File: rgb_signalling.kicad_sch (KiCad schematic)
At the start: 7 parts, among them IC1 TXB0108PWR

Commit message: working on board
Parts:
- C2, C3, C4: footprint (none) -> Capacitor_SMD:C_0504_1310Metric_Pad0.83x1.28mm_HandSolder
- renumbered D1 to D2, D2 to D3, D3 to D4
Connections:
- no-connect marks 9 -> 15
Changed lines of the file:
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@@
+	)
+	(no_connect
+		(at 154.94 55.88)
 	)
 	(no_connect
@@
 	)
 	(no_connect
+		(at 154.94 53.34)
+	)
+	(no_connect
+		(at 154.94 45.72)
+	)
+	(no_connect
+		(at 154.94 48.26)
+	)
+	(no_connect
 		(at 127 40.64)
+	)
+	(no_connect
+		(at 154.94 43.18)
 	)
 	(no_connect
 		(at 154.94 40.64)
+	)
+	(no_connect
+		(at 154.94 50.8)
 	)
 	(no_connect
@@
 		(dnp no)
 		(fields_autoplaced yes)
-		(property "Reference" "#PWR07"
+		(property "Reference" "#PWR09"
 			(at 156.21 120.65 0)
 			(effects
@@
 			(project "edge_human_detection_board"
 				(path "/f7edb1cc-a42a-4cc0-9a6f-d9bd2b944353/381303fc-36c2-4b05-8887-9e7cf2e23d0c"
-					(reference "#PWR07")
+					(reference "#PWR09")
 					(unit 1)
 				)
@@
 	(symbol
 		(lib_id "Device:C")
-		(at 198.12 111.76 180)
+		(at 175.26 92.71 180)
 		(unit 1)
 		(exclude_from_sim no)
@@
 		(dnp no)
 		(fields_autoplaced yes)
-		(property "Reference" "C4"
-			(at 201.93 110.4899 0)
+		(property "Reference" "C3"
+			(at 179.07 91.4399 0)
 			(effects
 				(font
@@
 		)
 		(property "Value" "0.1uF"
-			(at 201.93 113.0299 0)
+			(at 179.07 93.9799 0)
 			(effects
 				(font
@@
 			)
 		)
-		(property "Footprint" ""
-			(at 197.1548 107.95 0)
+		(property "Footprint" "Capacitor_SMD:C_0504_1310Metric_Pad0.83x1.28mm_HandSolder"
+			(at 174.2948 88.9 0)
 			(effects
 				(font
@@
 		)
 		(property "Datasheet" "~"
-			(at 198.12 111.76 0)
+			(at 175.26 92.71 0)
 			(effects
 				(font
@@
 		)
 		(property "Description" "Unpolarized capacitor"
-			(at 198.12 111.76 0)
+			(at 175.26 92.71 0)
 			(effects
 				(font
@@
 			(project "edge_human_detection_board"
 				(path "/f7edb1cc-a42a-4cc0-9a6f-d9bd2b944353/381303fc-36c2-4b05-8887-9e7cf2e23d0c"
-					(reference "C4")
+					(reference "C3")
 					(unit 1)
 				)
@@
 		(dnp no)
 		(fields_autoplaced yes)
-		(property "Reference" "#PWR08"
+		(property "Reference" "#PWR011"
 			(at 179.07 139.7 0)
 			(effects
@@
 			(project "edge_human_detection_board"
 				(path "/f7edb1cc-a42a-4cc0-9a6f-d9bd2b944353/381303fc-36c2-4b05-8887-9e7cf2e23d0c"
-					(reference "#PWR08")
+					(reference "#PWR011")
 					(unit 1)
 				)
@@
 		(dnp no)
 		(fields_autoplaced yes)
-		(property "Reference" "D3"
+		(property "Reference" "D4"
 			(at 190.5 114.3314 0)
 			(effects
@@
 			(project "edge_human_detection_board"
 				(path "/f7edb1cc-a42a-4cc0-9a6f-d9bd2b944353/381303fc-36c2-4b05-8887-9e7cf2e23d0c"
-					(reference "D3")
-					(unit 1)
-				)
-			)
-		)
-	)
-	(symbol
-		(lib_id "Device:C")
-		(at 175.26 92.71 180)
-		(unit 1)
-		(exclude_from_sim no)
-		(in_bom yes)
-		(on_board yes)
-		(dnp no)
-		(fields_autoplaced yes)
-		(property "Reference" "C3"
-			(at 179.07 91.4399 0)
-			(effects
-				(font
-					(size 1.27 1.27)
-				)
-				(justify right)
-			)
-		)
-		(property "Value" "0.1uF"
-			(at 179.07 93.9799 0)
-			(effects
-				(font
-					(size 1.27 1.27)
-				)
-				(justify right)
-			)
-		)
-		(property "Footprint" ""
-			(at 174.2948 88.9 0)
-			(effects
-				(font
-					(size 1.27 1.27)
-				)
-				(hide yes)
-			)
-		)
-		(property "Datasheet" "~"
-			(at 175.26 92.71 0)
-			(effects
-				(font
-					(size 1.27 1.27)
-				)
-				(hide yes)
-			)
-		)
-		(property "Description" "Unpolarized capacitor"
-			(at 175.26 92.71 0)
-			(effects
-				(font
-					(size 1.27 1.27)
-				)
-				(hide yes)
-			)
-		)
-		(pin "1"
-		)
-		(pin "2"
-		)
-		(instances
-			(project "edge_human_detection_board"
-				(path "/f7edb1cc-a42a-4cc0-9a6f-d9bd2b944353/381303fc-36c2-4b05-8887-9e7cf2e23d0c"
-					(reference "C3")
+					(reference "D4")
 					(unit 1)
 				)
@@
 		(dnp no)
 		(fields_autoplaced yes)
-		(property "Reference" "D2"
+		(property "Reference" "D3"
 			(at 167.64 95.2814 0)
 			(effects
@@
 			(project "edge_human_detection_board"
 				(path "/f7edb1cc-a42a-4cc0-9a6f-d9bd2b944353/381303fc-36c2-4b05-8887-9e7cf2e23d0c"
-					(reference "D2")
+					(reference "D3")
 					(unit 1)
 				)
@@
 		(dnp no)
 		(fields_autoplaced yes)
-		(property "Reference" "#PWR011"
+		(property "Reference" "#PWR012"
 			(at 198.12 124.46 0)
 			(effects
@@
 			(project "edge_human_detection_board"
 				(path "/f7edb1cc-a42a-4cc0-9a6f-d9bd2b944353/381303fc-36c2-4b05-8887-9e7cf2e23d0c"
-					(reference "#PWR011")
+					(reference "#PWR012")
+					(unit 1)
+				)
+			)
+		)
+	)
+	(symbol
+		(lib_id "Device:C")
+		(at 198.12 111.76 180)
+		(unit 1)
+		(exclude_from_sim no)
+		(in_bom yes)
+		(on_board yes)
+		(dnp no)
+		(fields_autoplaced yes)
+		(property "Reference" "C4"
+			(at 201.93 110.4899 0)
+			(effects
+				(font
+					(size 1.27 1.27)
+				)
+				(justify right)
+			)
+		)
+		(property "Value" "0.1uF"
+			(at 201.93 113.0299 0)
+			(effects
+				(font
+					(size 1.27 1.27)
+				)
+				(justify right)
+			)
+		)
+		(property "Footprint" "Capacitor_SMD:C_0504_1310Metric_Pad0.83x1.28mm_HandSolder"
+			(at 197.1548 107.95 0)
+			(effects
+				(font
+					(size 1.27 1.27)
+				)
+				(hide yes)
+			)
+		)
+		(property "Datasheet" "~"
+			(at 198.12 111.76 0)
+			(effects
+				(font
+					(size 1.27 1.27)
+				)
+				(hide yes)
+			)
+		)
+		(property "Description" "Unpolarized capacitor"
+			(at 198.12 111.76 0)
+			(effects
+				(font
+					(size 1.27 1.27)
+				)
+				(hide yes)
+			)
+		)
+		(pin "1"
+		)
+		(pin "2"
+		)
+		(instances
+			(project "edge_human_detection_board"
+				(path "/f7edb1cc-a42a-4cc0-9a6f-d9bd2b944353/381303fc-36c2-4b05-8887-9e7cf2e23d0c"
+					(reference "C4")
 					(unit 1)
 				)
@@
 		(dnp no)
 		(fields_autoplaced yes)
-		(property "Reference" "#PWR05"
+		(property "Reference" "#PWR06"
 			(at 118.11 46.99 0)
 			(effects
@@
 			(project ""
 				(path "/f7edb1cc-a42a-4cc0-9a6f-d9bd2b944353/381303fc-36c2-4b05-8887-9e7cf2e23d0c"
-					(reference "#PWR05")
+					(reference "#PWR06")
 					(unit 1)
 				)
@@
 		(dnp no)
 		(fields_autoplaced yes)
-		(property "Reference" "#PWR06"
+		(property "Reference" "#PWR07"
 			(at 130.81 106.68 0)
 			(effects
@@
 			(project "edge_human_detection_board"
 				(path "/f7edb1cc-a42a-4cc0-9a6f-d9bd2b944353/381303fc-36c2-4b05-8887-9e7cf2e23d0c"
-					(reference "#PWR06")
+					(reference "#PWR07")
 					(unit 1)
 				)
@@
 		(dnp no)
 		(fields_autoplaced yes)
-		(property "Reference" "D1"
+		(property "Reference" "D2"
 			(at 142.24 81.3114 0)
 			(effects
@@
 			(project "edge_human_detection_board"
 				(path "/f7edb1cc-a42a-4cc0-9a6f-d9bd2b944353/381303fc-36c2-4b05-8887-9e7cf2e23d0c"
-					(reference "D1")
+					(reference "D2")
 					(unit 1)
 				)
@@
 			)
 		)
-		(property "Footprint" ""
+		(property "Footprint" "Capacitor_SMD:C_0504_1310Metric_Pad0.83x1.28mm_HandSolder"
 			(at 148.8948 73.66 0)
 			(effects
@@
 		(dnp no)
 		(fields_autoplaced yes)
-		(property "Reference" "#PWR09"
+		(property "Reference" "#PWR08"
 			(at 149.86 90.17 0)
 			(effects
@@
 			(project "edge_human_detection_board"
 				(path "/f7edb1cc-a42a-4cc0-9a6f-d9bd2b944353/381303fc-36c2-4b05-8887-9e7cf2e23d0c"
-					(reference "#PWR09")
+					(reference "#PWR08")
 					(unit 1)
 				)

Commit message: made board
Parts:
- added TP1, TP2, TP3, TP4, TP5, TP6, TP7, TP8: TestPoint, TestPoint:TestPoint_Pad_D2.0mm, symbol Connector:TestPoint
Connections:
- net GND: now also TP5.1, TP6.1, TP7.1, TP8.1
- net PWM_0: now also TP1.1
- net SIG_IN_RGB1: now reaches D2.4 (DIN), IC1.20 (B1)
- net SIG_IN_RGB1: now also TP2.1
- net SIG_IN_RGB3: now reaches D3.2 (DOUT), D4.4 (DIN)
- net SIG_IN_RGB3: now also TP4.1
- net SIG_IN_RGB2: now reaches D2.2 (DOUT), D3.4 (DIN)
- net SIG_IN_RGB2: now also TP3.1
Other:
- note added: "RGB CIRCUIT"
- note added: "TEST POINTS"
- note removed: "I: 60 mA @ 5V"
- moved on the sheet: C2, C3, C4, D2, D3, D4, IC1

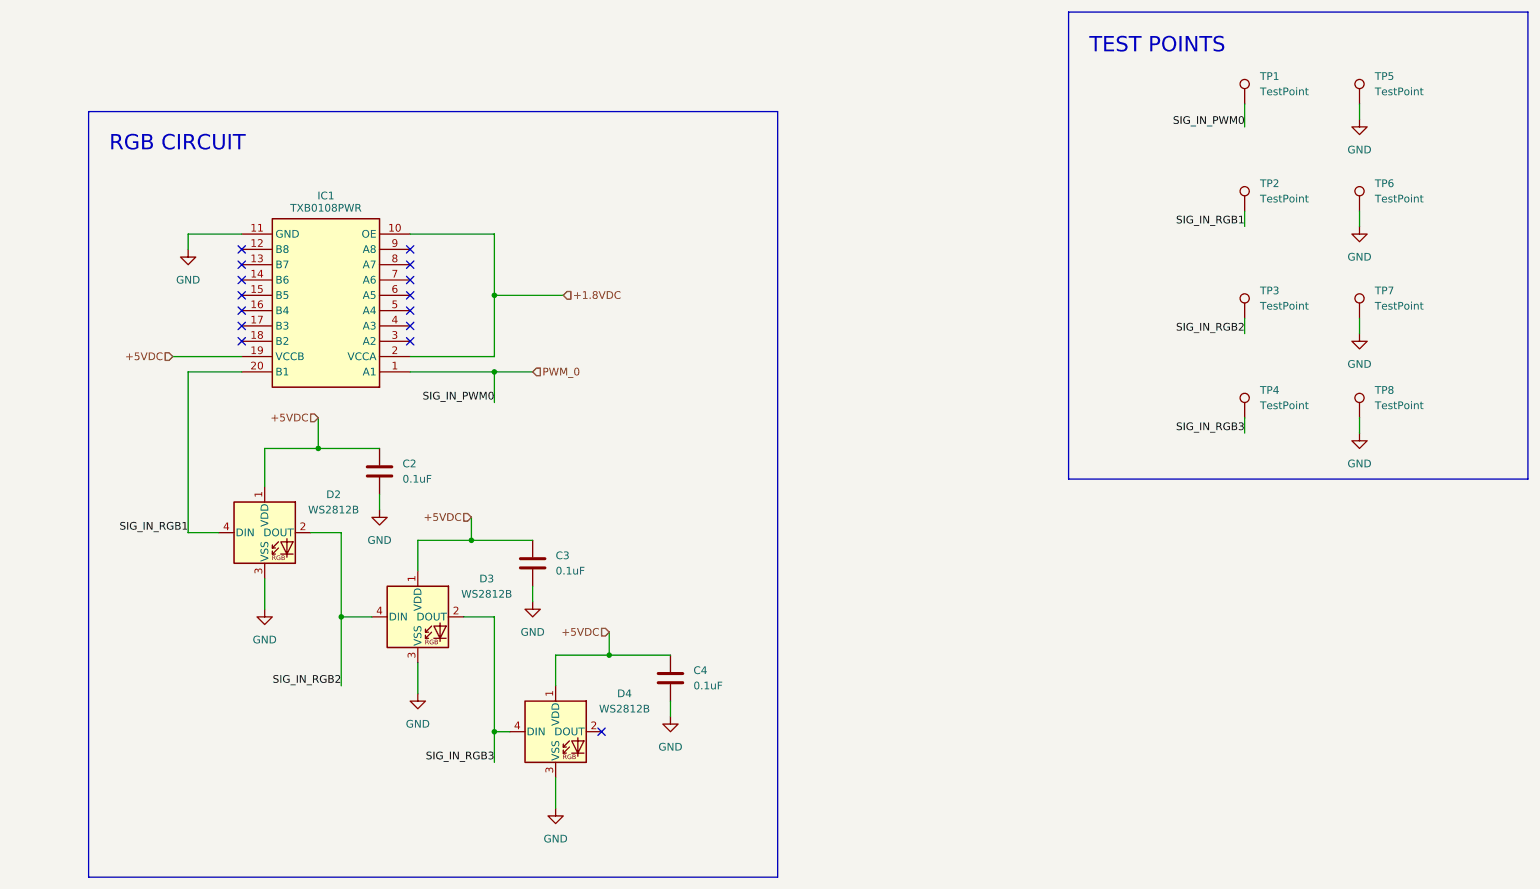
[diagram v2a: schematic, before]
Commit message: working on revisions
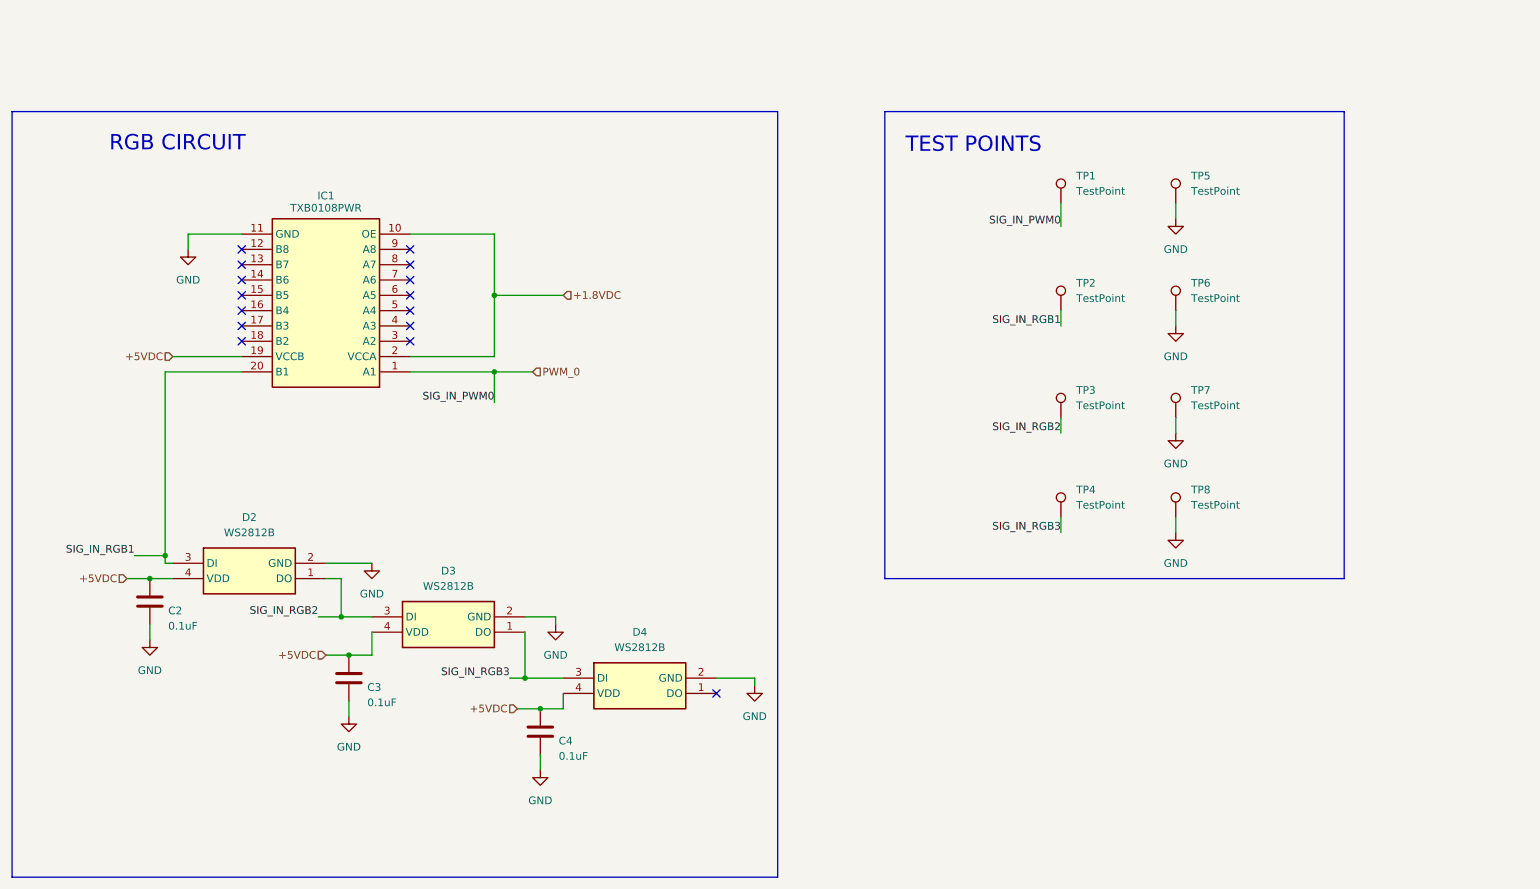
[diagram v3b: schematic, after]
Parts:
- removed D3, D4: WS2812B, LED_SMD:LED_WS2812B_PLCC4_5.0x5.0mm_P3.2mm, symbol LED:WS2812B
- added D3, D4: WS2812B, 4684, symbol 00_project_parts:4684
- D2: footprint LED_SMD:LED_WS2812B_PLCC4_5.0x5.0mm_P3.2mm -> 4684; symbol LED:WS2812B -> 00_project_parts:4684; Height (none) -> 0.84; Manufacturer_Name (none) -> Adafruit; Manufacturer_Part_Number (none) -> 4684; Mouser Part Number (none) -> 485-4684; Mouser Price/Stock (none) -> https://www.mouser.co.uk/ProductDetail/Adafruit/4684?qs=DPo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
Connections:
- net +5VDC: now also D2.4 (VDD), D3.4 (VDD), D4.4 (VDD); no longer D2.1 (VDD)
- net GND: now also D2.2 (GND), D3.2 (GND), D4.2 (GND); no longer D2.3 (VSS)
- net SIG_IN_RGB1: now also D2.3 (DI); no longer D2.4 (DIN)
- net SIG_IN_RGB2: now also D2.1 (DO), D3.3 (DI); no longer D2.2 (DOUT)
- net SIG_IN_RGB3: now also D3.1 (DO), D4.3 (DI)
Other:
- moved on the sheet: TP1, TP2, TP3, TP4, TP5, TP6, TP7, TP8

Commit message: Fab v
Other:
- note added: "I = 12 ma"
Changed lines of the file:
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@@
+		)
+	)
+	(text "I = 12 ma"
+		(exclude_from_sim no)
+		(at 77.978 125.984 0)
+		(effects
+			(font
+				(size 1.27 1.27)
+				(color 255 22 252 1)
+			)
+		)
+	)
+	(text "I = 12 ma"
+		(exclude_from_sim no)
+		(at 43.434 113.538 0)
+		(effects
+			(font
+				(size 1.27 1.27)
+				(color 255 22 252 1)
+			)
 		)
 	)
@@
 			)
 		)
+	)
+	(text "I = 12 ma"
+		(exclude_from_sim no)
+		(at 109.474 135.128 0)
+		(effects
+			(font
+				(size 1.27 1.27)
+				(color 255 22 252 1)
+			)
+		)

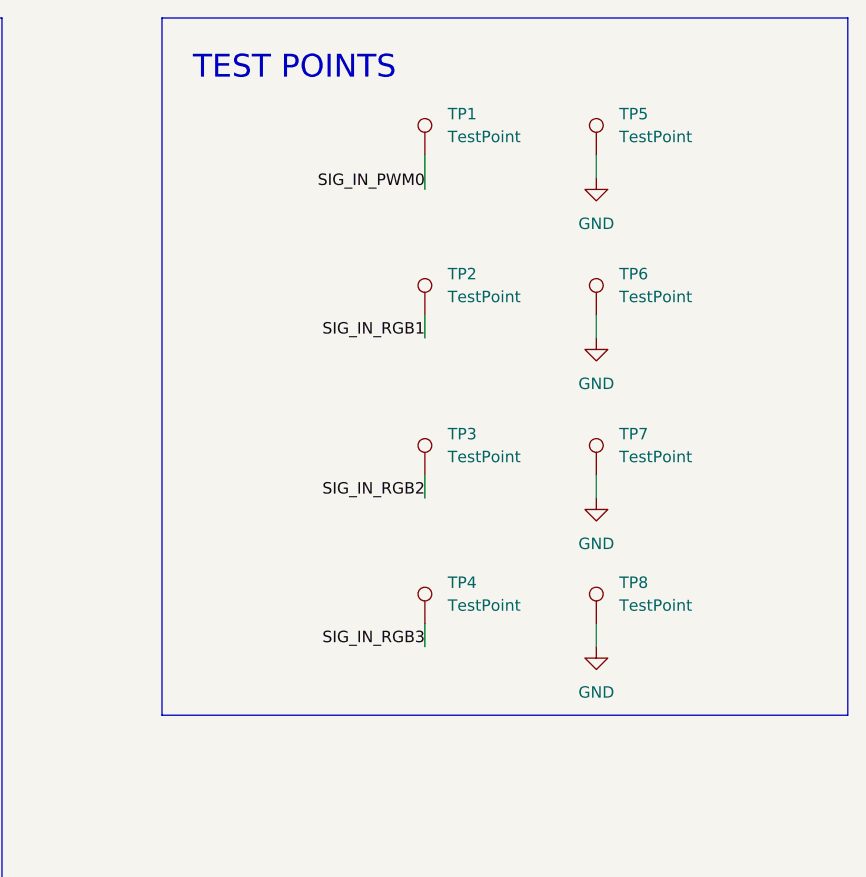
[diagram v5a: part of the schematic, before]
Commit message: not working, reverting to old design
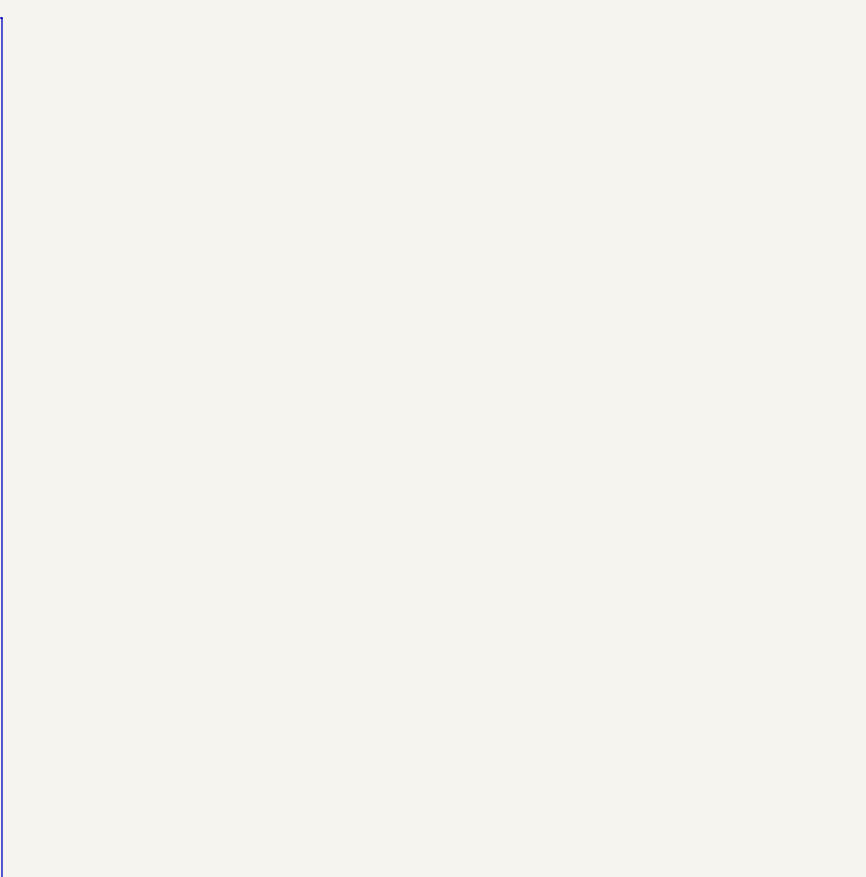
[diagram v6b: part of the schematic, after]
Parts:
- removed TP1, TP2, TP3, TP4, TP5, TP6, TP7, TP8: TestPoint, TestPoint:TestPoint_Pad_D2.0mm, symbol Connector:TestPoint
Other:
- note removed: "TEST POINTS"
